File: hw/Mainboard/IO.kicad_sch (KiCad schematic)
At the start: 11 parts, among them U11 W65C21N, U12 W65C22N, U13 W65C21N

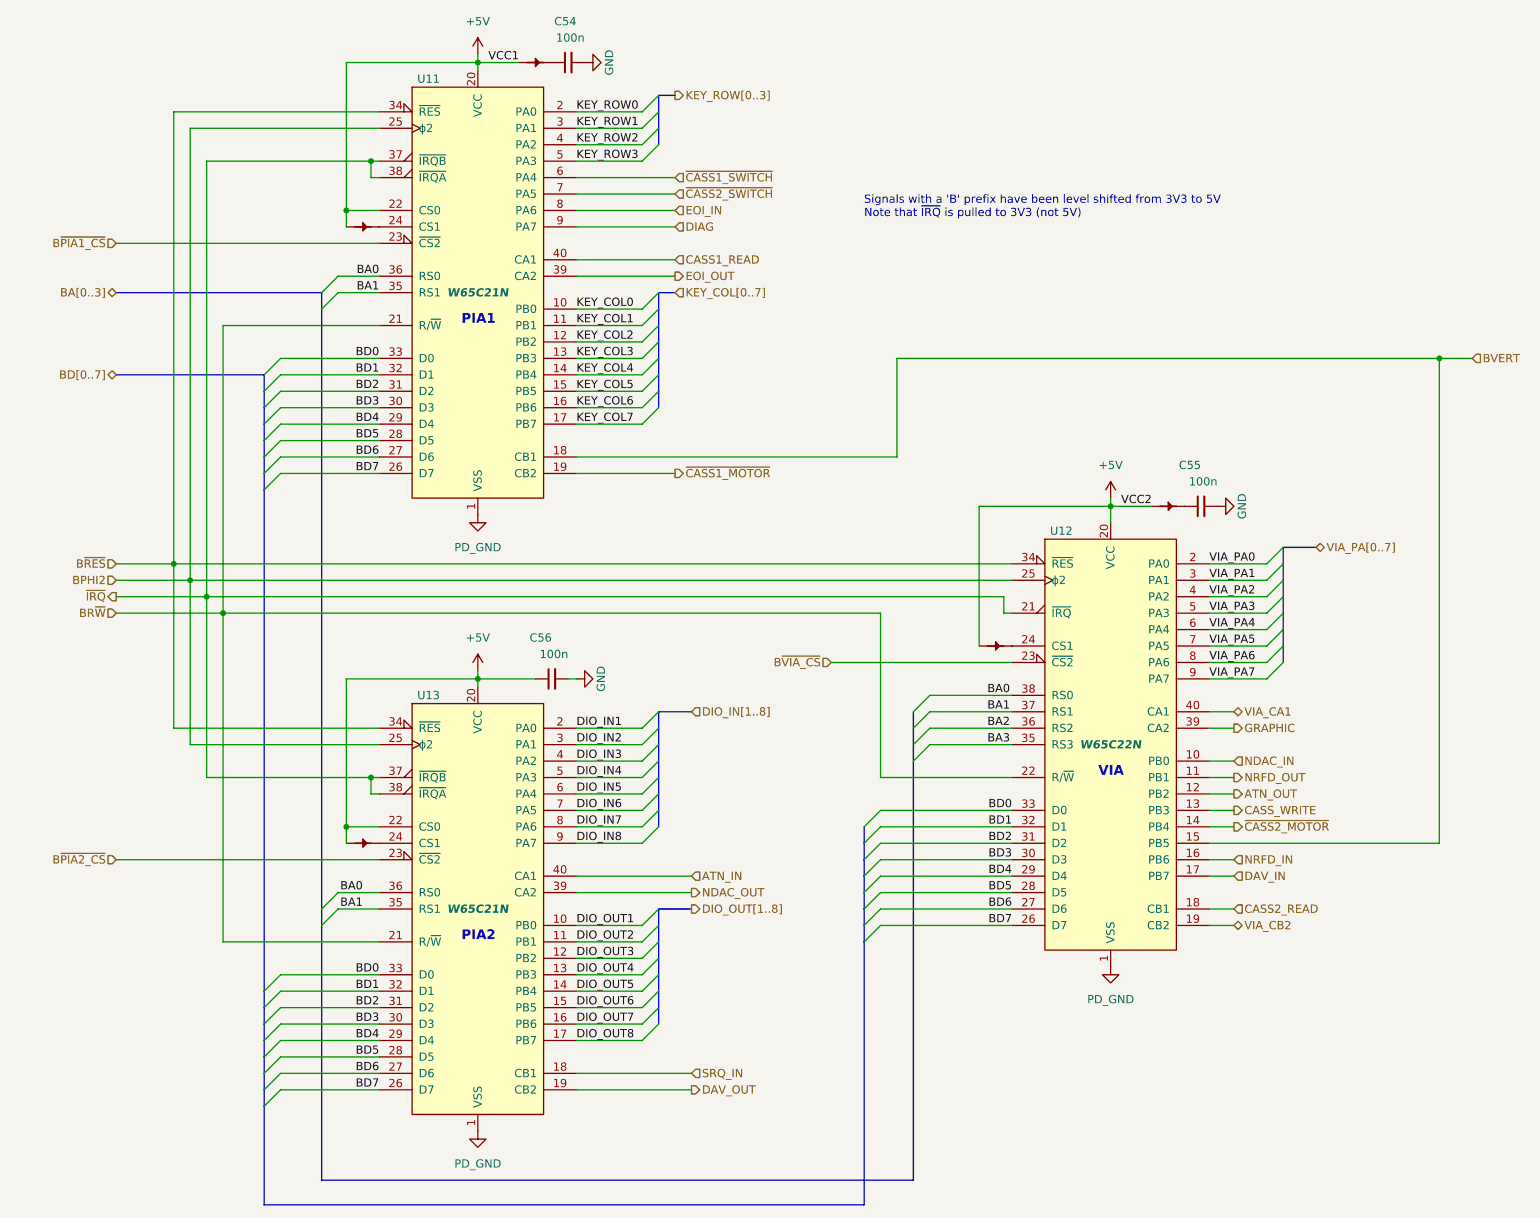
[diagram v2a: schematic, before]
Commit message: hw: routing touchups (wip)
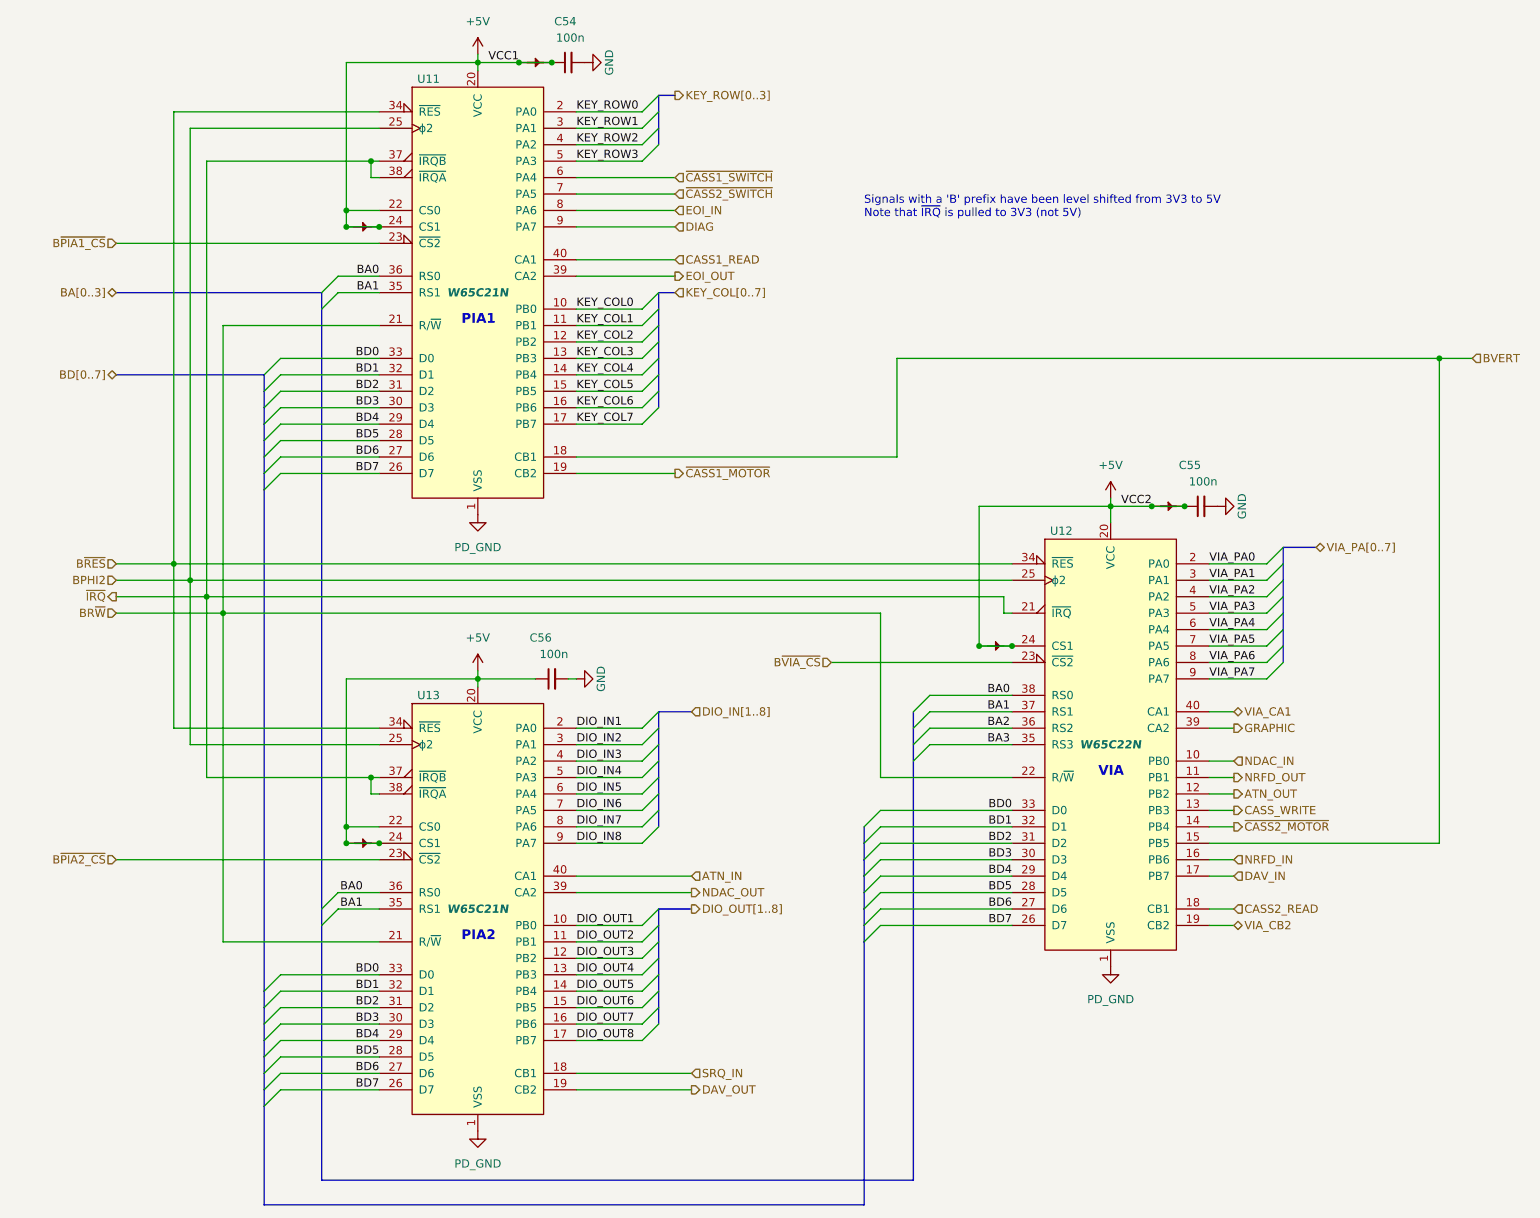
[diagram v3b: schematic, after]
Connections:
- net +5V: now also C54.1, C55.1, PT31.2, PT32.2, PT33.2, PT34.2, PT35.2, U11.24 (CS1), U12.24 (CS1), U13.24 (CS1)
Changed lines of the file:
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@@
   (junction (at 66.04 140.97) (diameter 0) (color 0 0 0 0)
   )
+  (junction (at 97.79 22.86) (diameter 0) (color 0 0 0 0)
+  )
+  (junction (at 71.12 48.26) (diameter 0) (color 0 0 0 0)
+  )
   (junction (at 184.15 91.44) (diameter 0) (color 0 0 0 0)
   )
+  (junction (at 92.71 22.86) (diameter 0) (color 0 0 0 0)
+  )
+  (junction (at 66.04 48.26) (diameter 0) (color 0 0 0 0)
+  )
   (junction (at 86.36 22.86) (diameter 0) (color 0 0 0 0)
   )
+  (junction (at 168.91 113.03) (diameter 0) (color 0 0 0 0)
+  )
   (junction (at 86.36 118.11) (diameter 0) (color 0 0 0 0)
   )
+  (junction (at 71.12 143.51) (diameter 0) (color 0 0 0 0)
+  )
   (junction (at 69.85 133.35) (diameter 0) (color 0 0 0 0)
   )
@@
   (junction (at 234.95 68.58) (diameter 0) (color 0 0 0 0)
   )
+  (junction (at 195.58 91.44) (diameter 0) (color 0 0 0 0)
+  )
   (junction (at 41.91 102.87) (diameter 0) (color 0 0 0 0)
   )
+  (junction (at 163.83 113.03) (diameter 0) (color 0 0 0 0)
+  )
   (junction (at 66.04 45.72) (diameter 0) (color 0 0 0 0)
   )
+  (junction (at 66.04 143.51) (diameter 0) (color 0 0 0 0)
+  )
   (junction (at 46.99 107.95) (diameter 0) (color 0 0 0 0)
   )
+  (junction (at 190.5 91.44) (diameter 0) (color 0 0 0 0)
+  )
   (junction (at 39.37 100.33) (diameter 0) (color 0 0 0 0)
   )
@@
     (stroke (width 0) (type default) (color 0 0 0 0))
   )
+  (wire (pts (xy 66.04 143.51) (xy 71.12 143.51))
+    (stroke (width 0) (type default) (color 0 0 0 0))
+  )
   (wire (pts (xy 71.12 135.89) (xy 69.85 135.89))
     (stroke (width 0) (type default) (color 0 0 0 0))
@@
     (stroke (width 0) (type default) (color 0 0 0 0))
   )
+  (wire (pts (xy 66.04 48.26) (xy 71.12 48.26))
+    (stroke (width 0) (type default) (color 0 0 0 0))
+  )
   (bus (pts (xy 114.3 166.37) (xy 114.3 168.91))
     (stroke (width 0) (type default) (color 0 0 0 0))
@@
     (stroke (width 0) (type default) (color 0 0 0 0))
   )
+  (wire (pts (xy 163.83 113.03) (xy 168.91 113.03))
+    (stroke (width 0) (type default) (color 0 0 0 0))
+  )
   (bus (pts (xy 146.05 153.67) (xy 146.05 156.21))
     (stroke (width 0) (type default) (color 0 0 0 0))
@@
     (stroke (width 0) (type default) (color 0 0 0 0))
   )
+  (wire (pts (xy 92.71 22.86) (xy 97.79 22.86))
+    (stroke (width 0) (type default) (color 0 0 0 0))
+  )
   (wire (pts (xy 55.88 166.37) (xy 71.12 166.37))
     (stroke (width 0) (type default) (color 0 0 0 0))
@@
     (stroke (width 0) (type default) (color 0 0 0 0))
   )
+  (wire (pts (xy 190.5 91.44) (xy 195.58 91.44))
+    (stroke (width 0) (type default) (color 0 0 0 0))
+  )

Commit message: hw: caps & logos (wip)
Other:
- title: CBM PET Mainboard Replacement -> EconoPET 40/8096
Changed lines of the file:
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@@
   (paper "A")
   (title_block
-    (title "CBM PET Mainboard Replacement")
+    (title "EconoPET 40/8096")
+    (date "2023-10-01")
+    (rev "A")
   )
   (junction (at 66.04 140.97) (diameter 0) (color 0 0 0 0)
